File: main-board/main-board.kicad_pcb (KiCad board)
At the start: 2 copper layers, 101 x 101 mm, 72 parts, among them J1 C10418, J2 FH12-24S-0.5SH(55), J3 TF-01A, Q1 Q_NPN_BCE, Q2 Q_NPN_BCE, Q3 Q_NPN_BCE, Q4 DMG1012T, SW1 SW_DIP_x01, U1 ESP-32s, U2 HT7333-A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

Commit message: Small fixes
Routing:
- net GND: vias 69 -> 70
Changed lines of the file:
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@@
-(kicad_pcb (version 20171130) (host pcbnew "(5.1.4-0-10_14)")
+(kicad_pcb (version 20171130) (host pcbnew "(5.1.4)-1")
   (general
     (thickness 1.6)
     (drawings 1)
-    (tracks 884)
+    (tracks 885)
     (zones 0)
     (modules 72)
@@
   (via (at 125.4 54.4) (size 0.8) (drill 0.4) (layers F.Cu B.Cu) (net 6))
   (via (at 151.4 110.8) (size 0.8) (drill 0.4) (layers F.Cu B.Cu) (net 6))
+  (via (at 174.8 75.9) (size 0.8) (drill 0.4) (layers F.Cu B.Cu) (net 6) (status 1000000))
   (via (at 189.75 103) (size 0.8) (drill 0.4) (layers F.Cu B.Cu) (net 7))
   (segment (start 160.573372 121.873372) (end 159.95 121.25) (width 0.25) (layer F.Cu) (net 7))

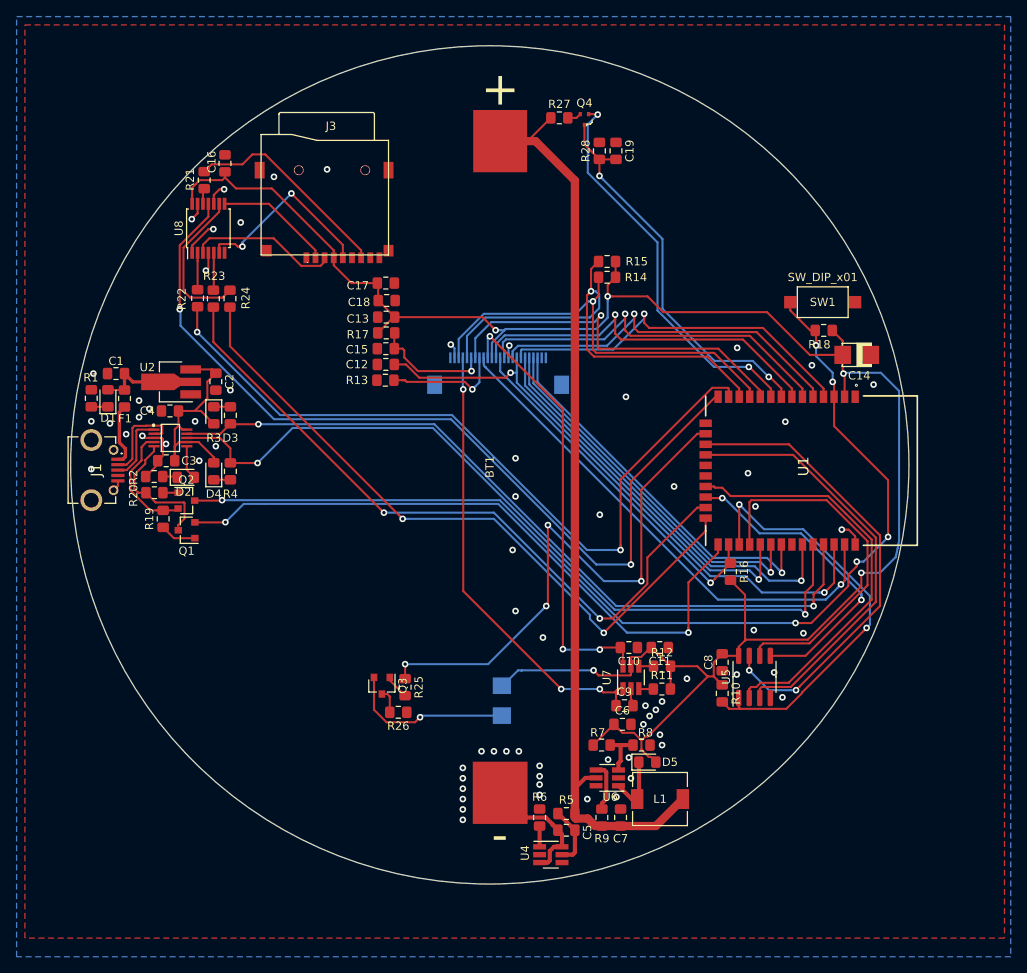
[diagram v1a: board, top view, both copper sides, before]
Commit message: Mounting holes and test points
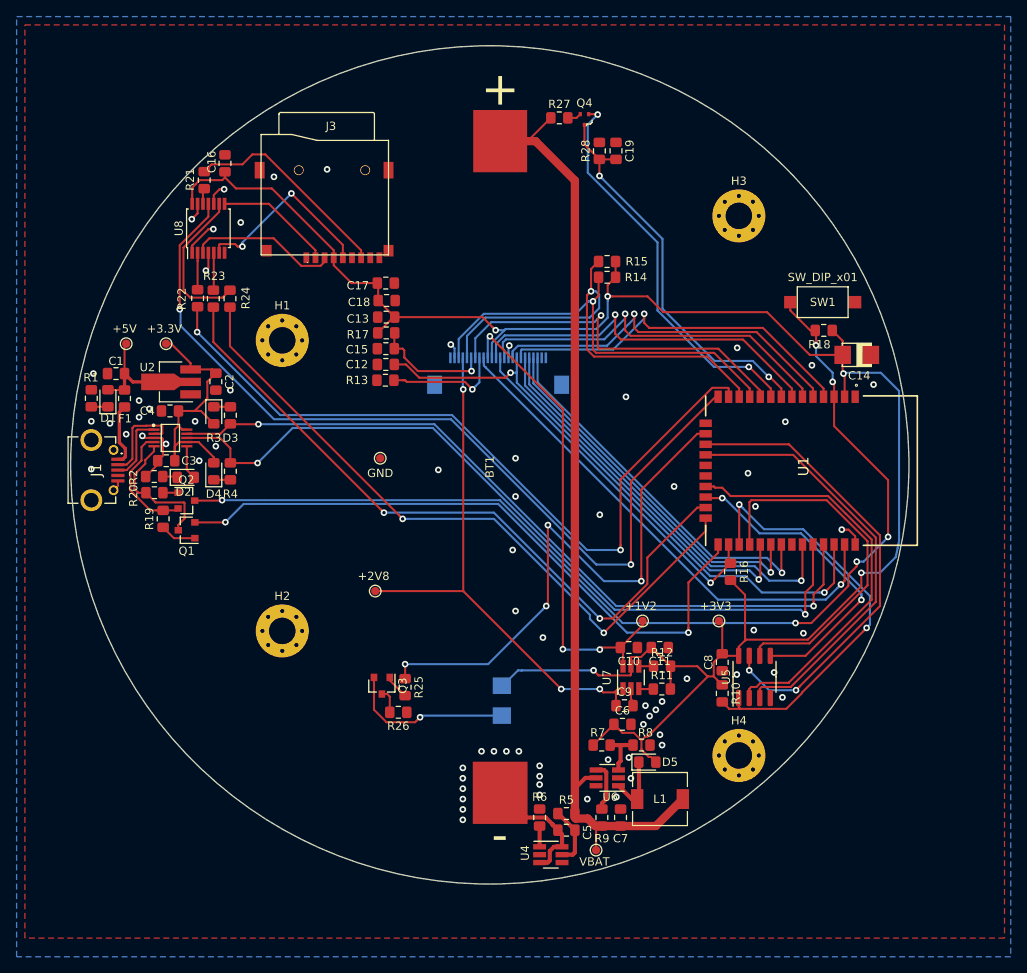
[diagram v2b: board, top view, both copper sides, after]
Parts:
- added H1: MountingHole, MountingHole:MountingHole_3.2mm_M3_Pad_Via, F.Cu at (120.0, 75.0)
- added H2: MountingHole, MountingHole:MountingHole_3.2mm_M3_Pad_Via, F.Cu at (120.0, 110.0)
- added H3: MountingHole, MountingHole:MountingHole_3.2mm_M3_Pad_Via, F.Cu at (175.0, 60.0)
- added H4: MountingHole, MountingHole:MountingHole_3.2mm_M3_Pad_Via, F.Cu at (175.0, 125.0)
- added TP1: +2V8, TestPoint:TestPoint_Pad_D1.0mm, F.Cu at (131.2, 105.2)
- added TP2: VBAT, TestPoint:TestPoint_Pad_D1.0mm, F.Cu at (157.8, 136.4)
- added TP3: GND, TestPoint:TestPoint_Pad_D1.0mm, F.Cu at (131.8, 89.2)
- added TP4: +5V, TestPoint:TestPoint_Pad_D1.0mm, F.Cu at (101.2, 75.4)
- added TP5: +3.3V, TestPoint:TestPoint_Pad_D1.0mm, F.Cu at (106.0, 75.4)
- added TP6: +3V3, TestPoint:TestPoint_Pad_D1.0mm, F.Cu at (172.6, 108.8)
- added TP7: +1V2, TestPoint:TestPoint_Pad_D1.0mm, F.Cu at (163.4, 108.8)
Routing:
- net +2V8: track 54.4 -> 65.0 mm
- net VCC: track 29.2 -> 33.9 mm
- net +1V2: track 53.5 -> 57.8 mm
- net +3V3: track 241.2 -> 245.3 mm
- net +5V: track 12.4 -> 16.0 mm
- net /VBAT: track 115.8 -> 118.8 mm
- net GND: vias 70 -> 71

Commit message: BOM parts
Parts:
- L1: footprint Inductor_SMD:L_6.3x6.3_H3 -> Inductor_SMD:L_7.3x7.3_H3.5
- moved D5 3.13 mm to (166.2, 123.6), turned to 90 degrees
- moved L1 0.72 mm to (165.8, 129.6)
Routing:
- net Net-(D5-Pad1): track 7.97 -> 10.3 mm
- net +3V3: track 245.3 -> 243.5 mm
- net /VBAT: track 118.8 -> 119.8 mm
- net GND: vias 71 -> 70

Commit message: BOM parts 2
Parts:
- C6, C7: footprint Capacitor_SMD:C_0805_2012Metric_Pad1.15x1.40mm_HandSolder -> Capacitor_SMD:C_1206_3216Metric_Pad1.42x1.75mm_HandSolder
- D5: footprint Diode_SMD:D_0805_2012Metric_Pad1.15x1.40mm_HandSolder -> Diode_SMD:D_SMA_Handsoldering
- L1: footprint Inductor_SMD:L_7.3x7.3_H3.5 -> Inductor_SMD:L_Bourns-SRN6028
- SW1: footprint Button_Switch_SMD:SW_SPST_CK_RS282G05A3 -> Button_Switch_SMD:SW_SPST_B3U-1000P
- moved SW1 5.16 mm to (189.3, 73.4)
- moved C6 2.13 mm to (161.6, 123.3), turned to 90 degrees
- moved D5 1.49 mm to (167.2, 122.5)
- moved R8 1.42 mm to (164.2, 124.8), turned to 90 degrees
- moved L1 1.26 mm to (165.4, 130.8)
- moved C7 0.61 mm to (160.8, 133.1)
- moved R18 0.42 mm to (184.8, 73.8)
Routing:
- net +3V3: track 243.5 -> 240.0 mm
- net Net-(R7-Pad2): track 5.85 -> 7.49 mm
- net /CSI_PWD: track 14.4 -> 15.1 mm
- net Net-(D5-Pad1): track 10.3 -> 11.0 mm
- net GND: vias 70 -> 71
